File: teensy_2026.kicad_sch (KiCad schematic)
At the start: 0 parts

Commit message: Added in the two I2C Buses and the LED
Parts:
- added U1: RASPBERRY_PI_PICO, RASPBERRY_PI_PICO:RASPBERRY_PI_PICO, symbol RASPBERRY_PI_PICO:RASPBERRY_PI_PICO
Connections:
- new net +3V3: U1.3V3
- new net GND: U1.AGND, U1.GND, U1.GND2, U1.GND3, U1.GND4, U1.GND5, U1.GND6, U1.GND7

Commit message: Forgot to commit
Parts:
- added J1: LED, LED_THT:LED_D5.0mm_IRGrey, symbol Connector:Conn_01x03_Pin
- added R1, R2, R3, R4: 10K, Resistor_THT:R_Array_SIP4, symbol Device:R_US
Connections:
- net +3V3: now also R1.1, R2.1, R3.1, R4.1
- net GND: now also J1.3 (Pin_3); no longer U1.AGND
- net SDA 1: now reaches U1.GP16
- net SDA 1: now also R4.2
- net SDA 0: now reaches U1.GP18
- net SDA 0: now also R2.2
- net SCL 0: now reaches U1.GP19
- net SCL 0: now also R1.2
- net LEDdata: now reaches U1.GP22
- net LEDdata: now also J1.1 (Pin_1)
- new net +5V: J1.2 (Pin_2)
- new net SCL 1: R3.2
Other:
- note added: "CURRENT SENSE"
- note added: "Other Inputs/Outputs"
- note added: "STRAIN GAUGE"

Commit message: Added Linear Actuator
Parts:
- added J3: LinearActSaber, teensy:3pinJST, symbol Connector:Conn_01x03_Pin
- added TP10: LinAct TX Testpoint, Connector_Wire:SolderWire-0.75sqmm_1x01_D1.25mm_OD2.3mm, symbol Connector:TestPoint
- added TP9: LinAct RX Testpoint, Connector_Wire:SolderWire-0.75sqmm_1x01_D1.25mm_OD2.3mm, symbol Connector:TestPoint
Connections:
- net GND: now also J3.3 (Pin_3)
- net Pico TX: now reaches U1.GP4
- net Pico RX: now reaches U1.GP5
- new net LinAct RX: J3.1 (Pin_1), TP9.1
- new net LinAct TX: J3.2 (Pin_2), TP10.1
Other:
- note added: "LinAct TX = Pico RX LinAct RX = Pico TX"
- moved on the sheet: J1

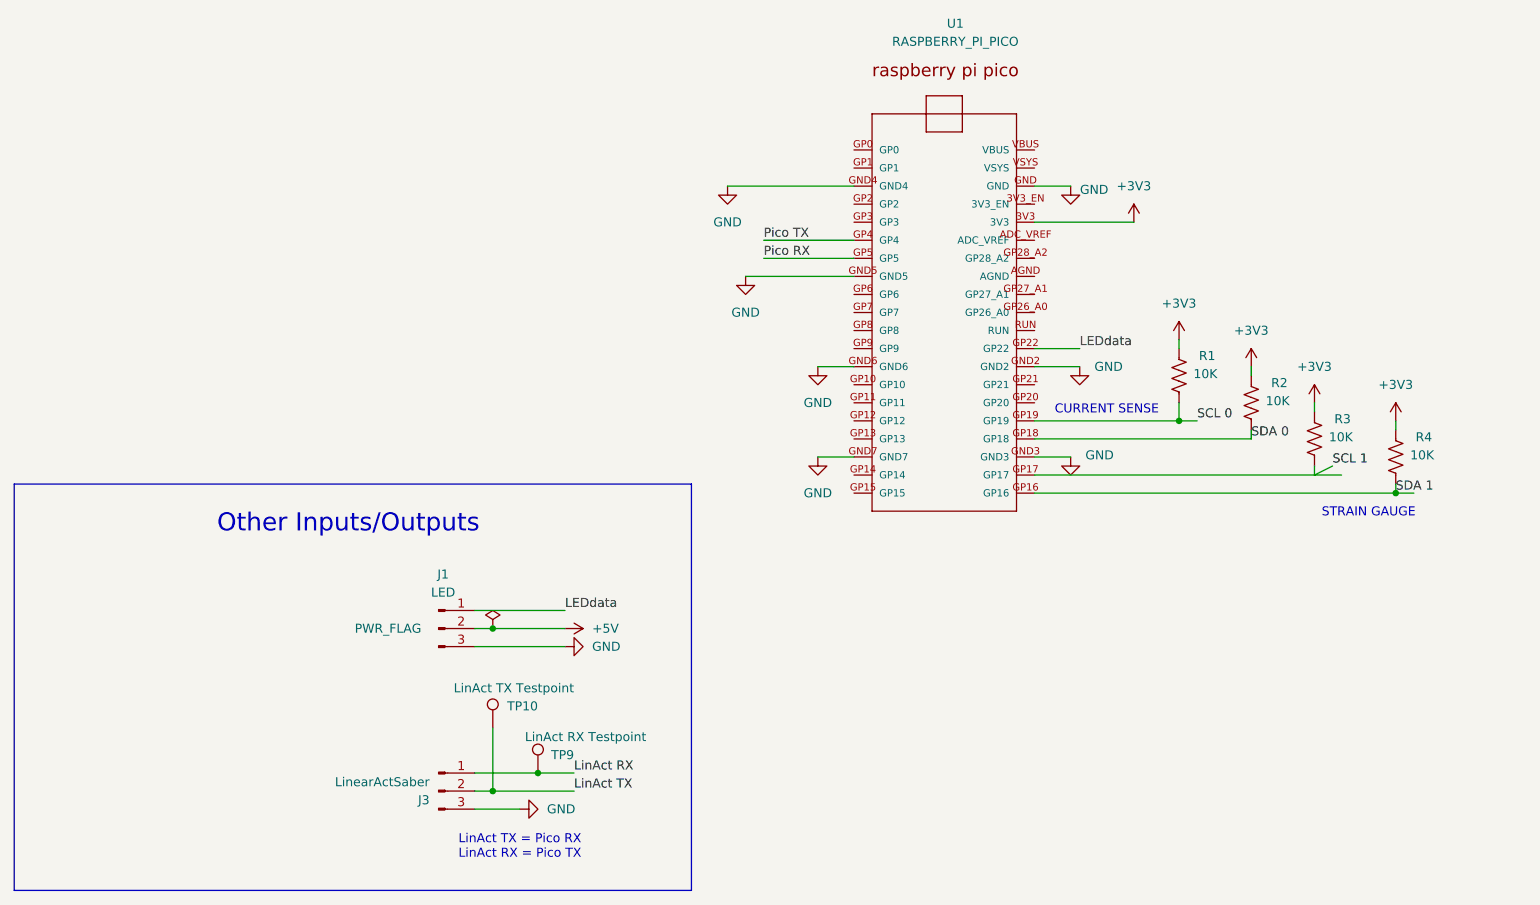
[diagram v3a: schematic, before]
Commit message: Added battery management system connectors but actually
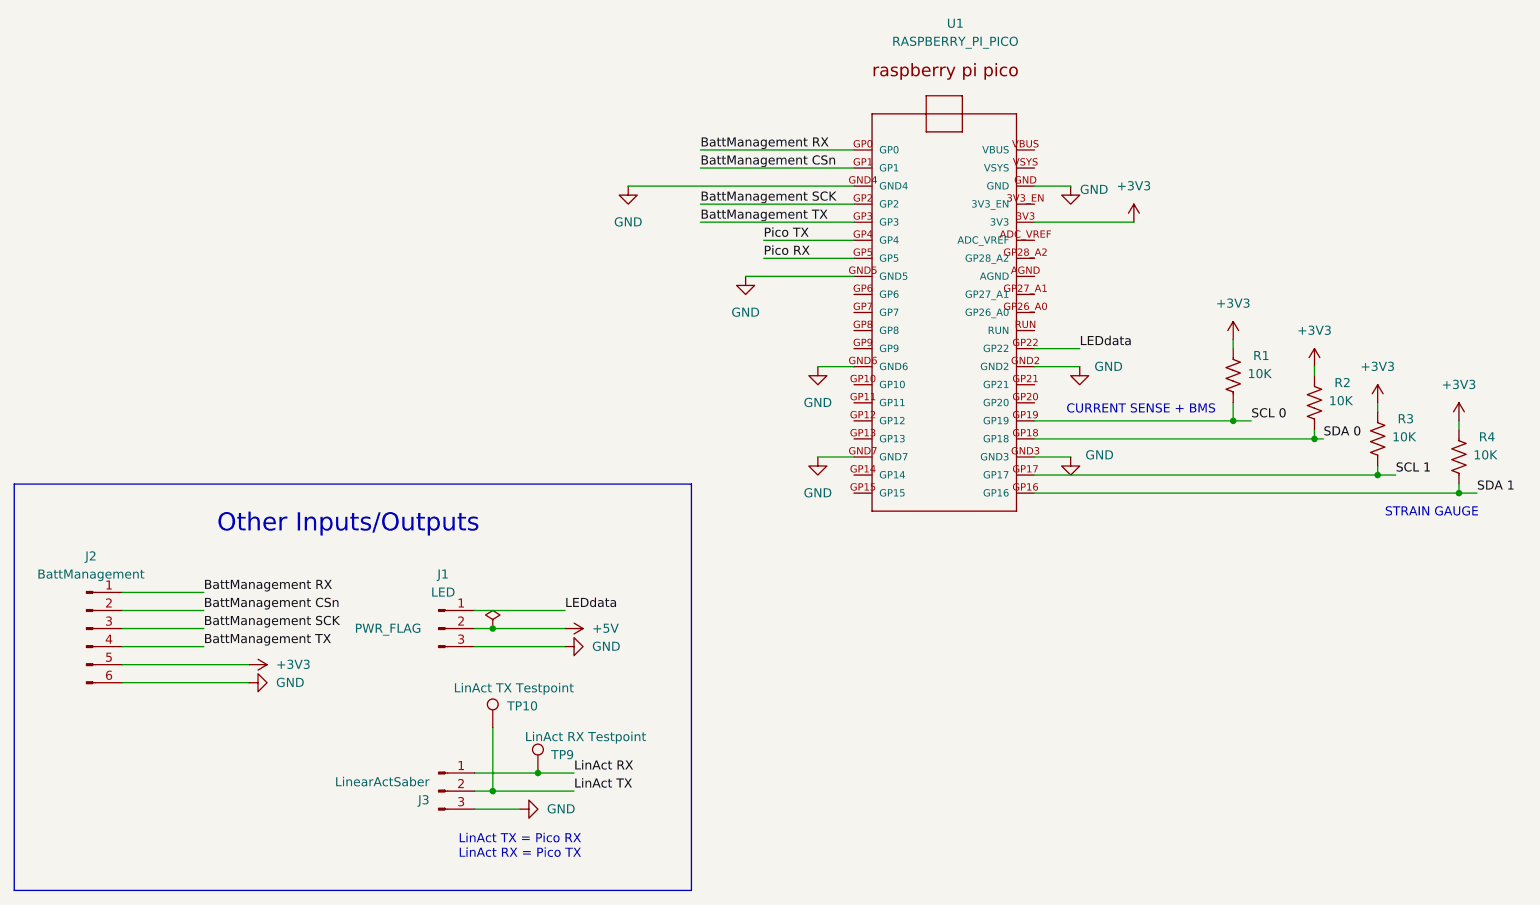
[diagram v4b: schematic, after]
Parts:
- added J2: BattManagement, symbol Connector:Conn_01x06_Pin
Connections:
- net +3V3: now also J2.5 (Pin_5)
- net GND: now also J2.6 (Pin_6)
- net SCL 1: now also U1.GP17
- net BattManagement RX: now reaches U1.GP0
- net BattManagement RX: now also J2.1 (Pin_1)
- net BattManagement CSn: now reaches U1.GP1
- net BattManagement CSn: now also J2.2 (Pin_2)
- net BattManagement SCK: now reaches U1.GP2
- net BattManagement SCK: now also J2.3 (Pin_3)
- net BattManagement TX: now reaches U1.GP3
- net BattManagement TX: now also J2.4 (Pin_4)
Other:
- note added: "CURRENT SENSE + BMS"
- note removed: "CURRENT SENSE"
- moved on the sheet: R1, R2, R3, R4
